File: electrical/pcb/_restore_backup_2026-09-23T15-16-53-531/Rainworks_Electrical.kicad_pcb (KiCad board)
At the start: 2 copper layers, 111.4 x 40.9 mm, 19 parts, among them J1 472192001, P1 ESP8266 Thing, U1 MCP3008, U10 S1_SM, U11 S0_PH, U7 S4_FR, U8 S3_T, U9 S2_C

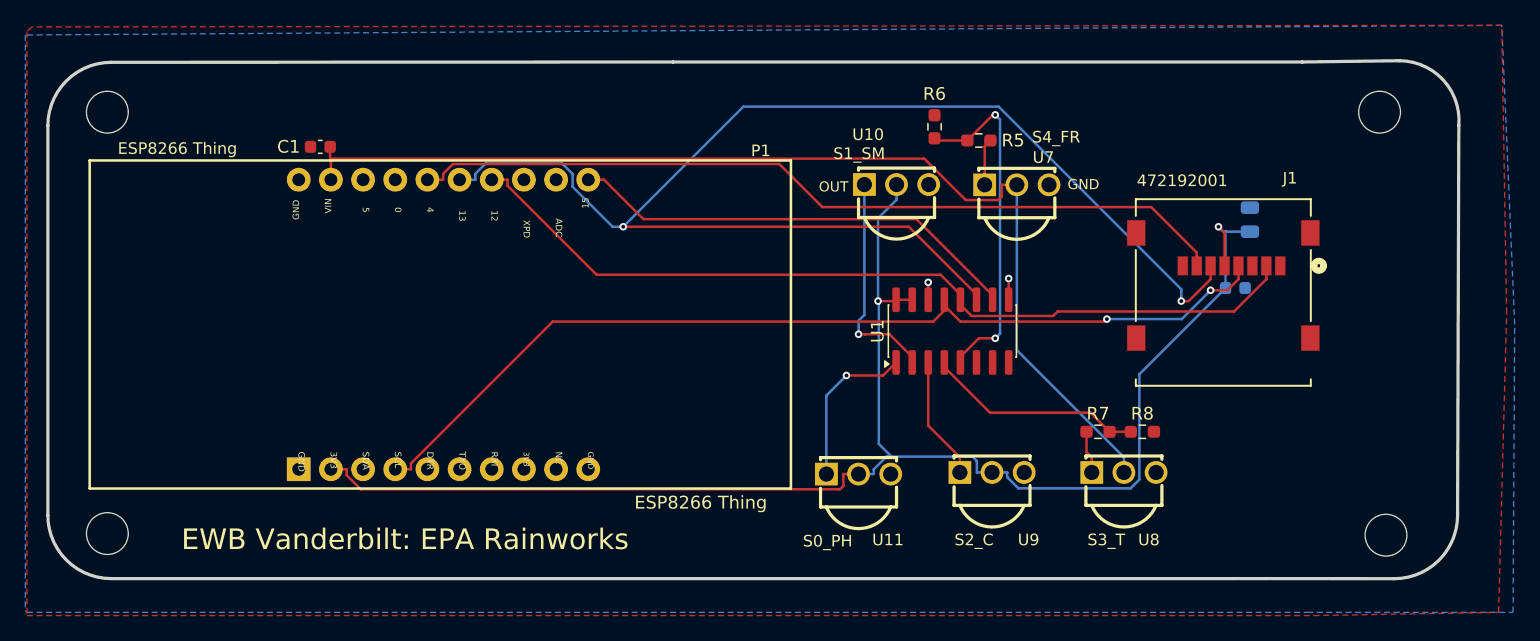
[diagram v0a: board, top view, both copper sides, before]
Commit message: fixed drc errors
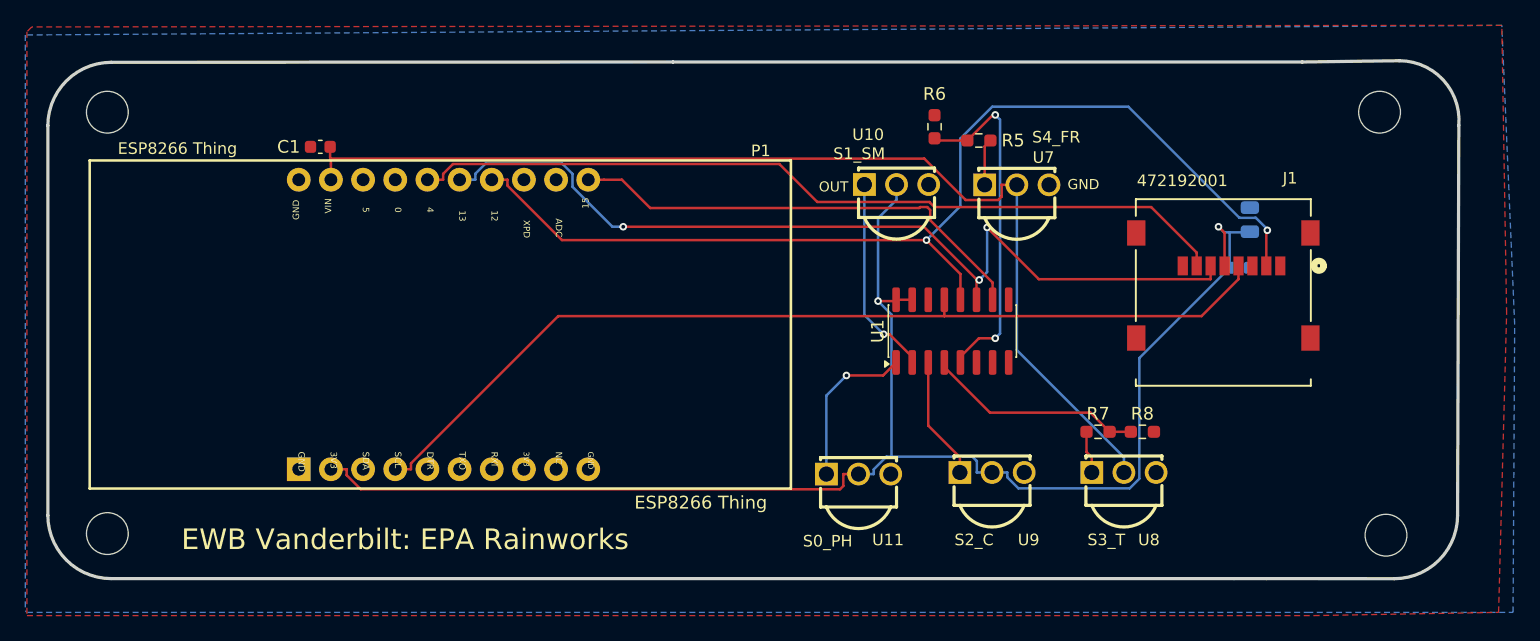
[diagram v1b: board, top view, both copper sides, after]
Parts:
- moved C2 1.63 mm to (191.1, 97.5)
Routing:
- net /SD_MOSI_SPI: track 105.9 -> 72.6 mm, vias 2 -> 3
- net /SD_MISO_SPI: track 68.6 -> 83.7 mm, vias 0 -> 2
- net GND: track 3.05 -> 0.00 mm, vias 2 -> 0
- net /CH1_ADC: track 17.4 -> 15.9 mm
- net Net-(P1-15): track 36.1 -> 37.2 mm
- net /SD_SCLK_SPI: track 75.9 -> 75.4 mm, vias 2 -> 0
